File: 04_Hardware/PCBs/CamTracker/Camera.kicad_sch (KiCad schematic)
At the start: 29 parts, among them J11 22-28-4034, J12 22-28-4034, J8 20021521-00016T1LF, J9 20021521-00016T1LF, U1 SC206EEMDA-G51-UGNDA

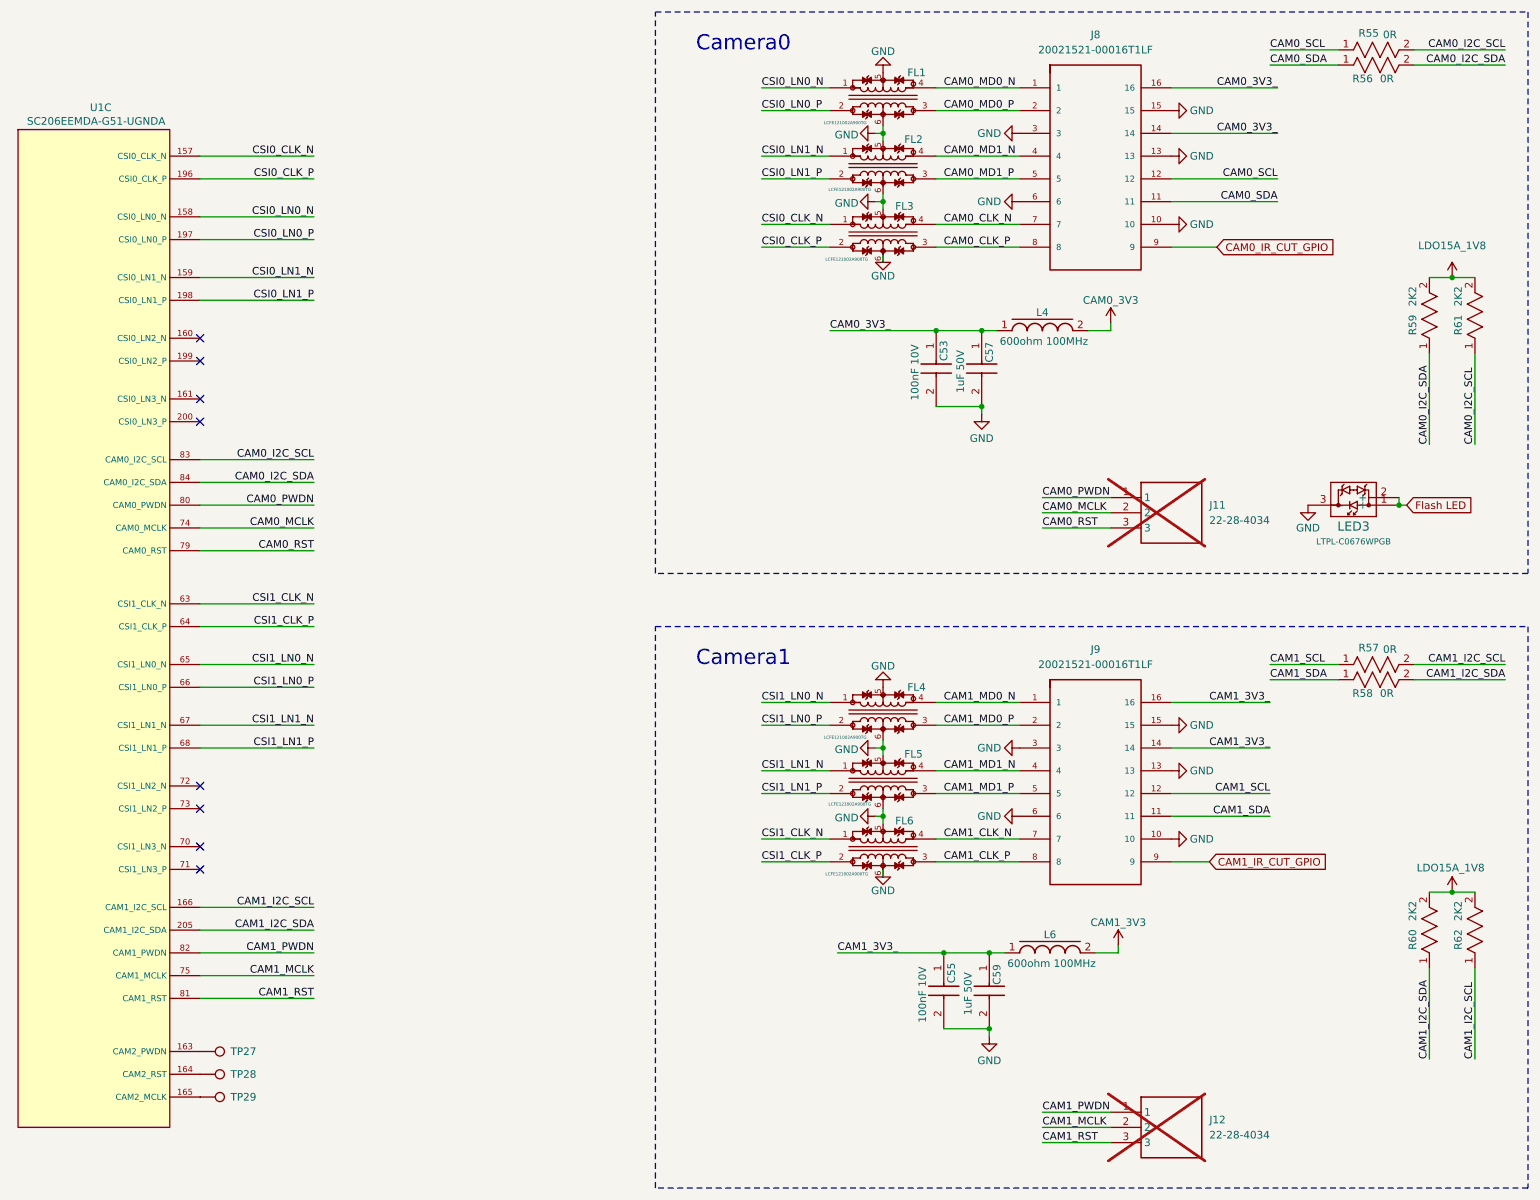
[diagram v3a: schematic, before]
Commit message: feat(PCB): Cam Connectors have been changed with 2x10P
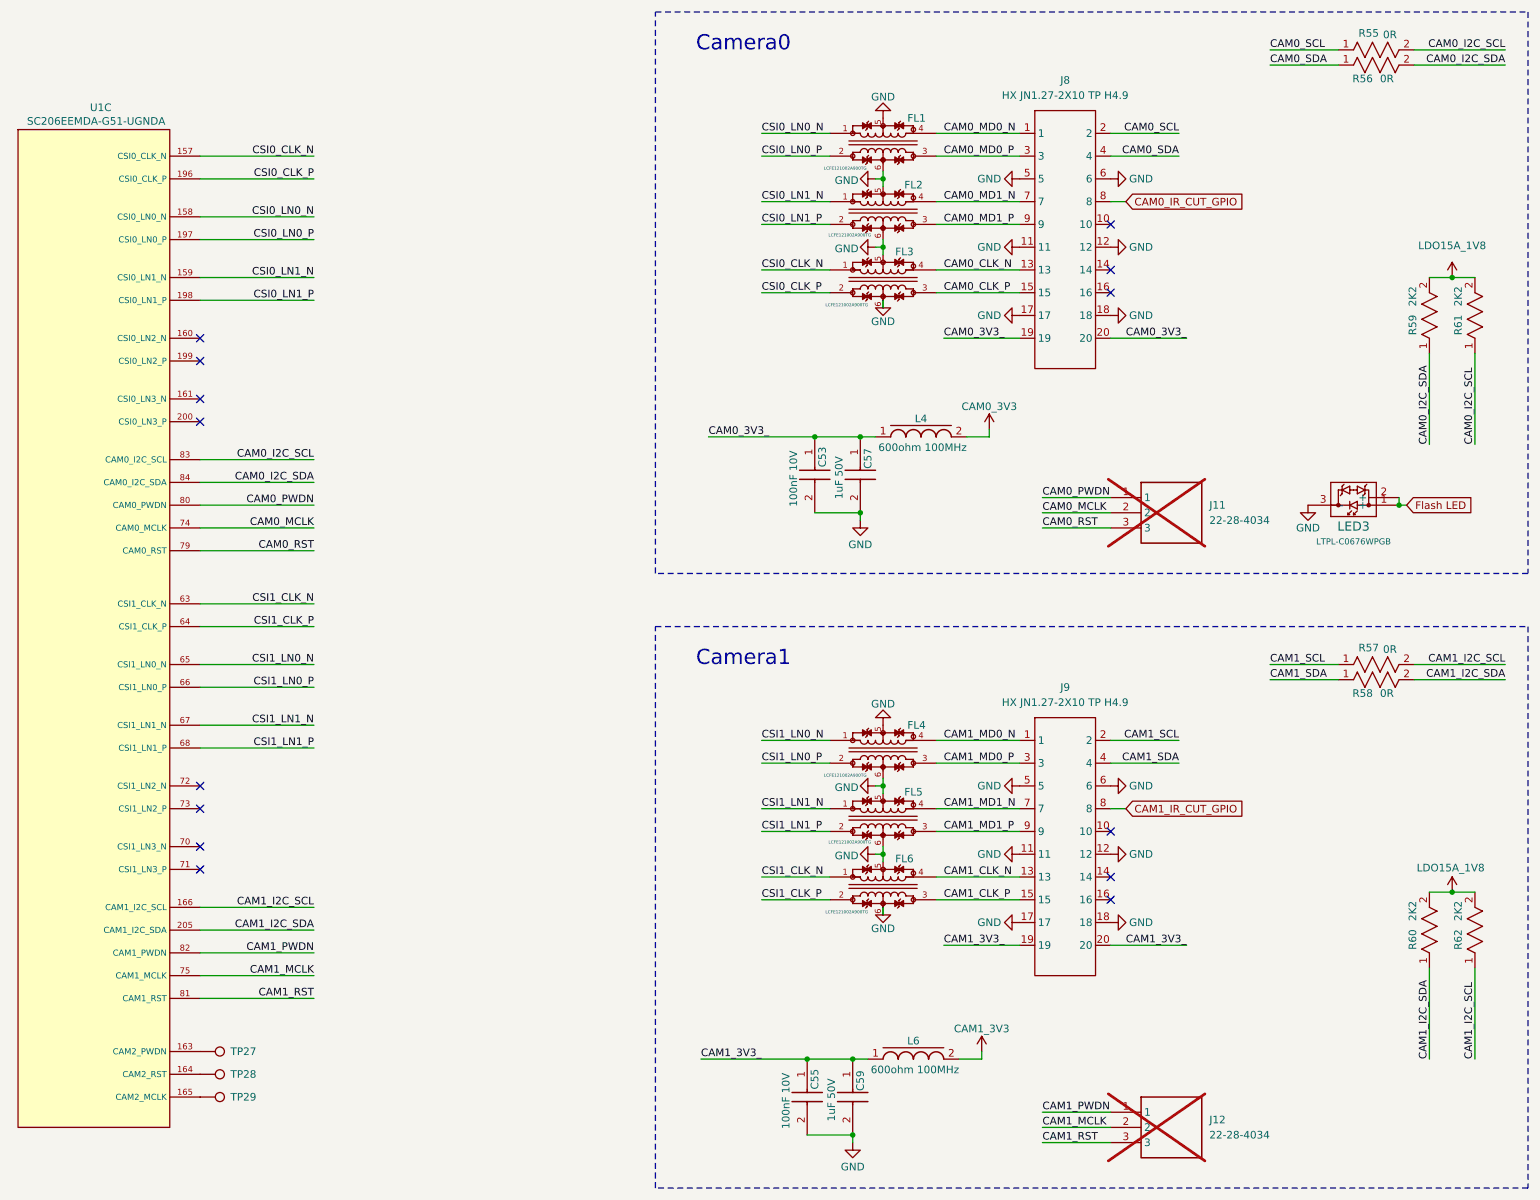
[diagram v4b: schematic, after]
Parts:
- removed J8, J9: 20021521-00016T1LF, 000MCLib:AMPHENOL_20021521-00016T1LF, symbol 000MCLib:20021521-00016T1LF
- added J8, J9: HX JN1.27-2X10 TP H4.9, 000MCLib:CONN-SMD_HX-JN1.27-2X10-TP-H4.9, symbol 000MCLib:HX JN1.27-2X10 TP H4.9
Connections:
- net CAM0_3V3_: now also J8.19, J8.20
- net CAM0_CLK_N: now also J8.13
- net CAM0_CLK_P: now also J8.15
- net CAM0_IR_CUT_GPIO: now also J8.8
- net CAM0_MD0_N: now also J8.1
- net CAM0_MD0_P: now also J8.3
- net CAM0_MD1_N: now also J8.7
- net CAM0_MD1_P: now also J8.9
- net CAM0_SCL: now also J8.2
- net CAM0_SDA: now also J8.4
- net CAM1_3V3_: now also J9.19, J9.20
- net CAM1_CLK_N: now also J9.13
- net CAM1_CLK_P: now also J9.15
- net CAM1_IR_CUT_GPIO: now also J9.8
- net CAM1_MD0_N: now also J9.1
- net CAM1_MD0_P: now also J9.3
- net CAM1_MD1_N: now also J9.7
- net CAM1_MD1_P: now also J9.9
- net CAM1_SCL: now also J9.2
- net CAM1_SDA: now also J9.4
- net GND: now also J8.11, J8.12, J8.17, J8.18, J8.5, J8.6, J9.11, J9.12, J9.17, J9.18, J9.5, J9.6
- no-connect marks 8 -> 14
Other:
- moved on the sheet: C53, C55, C57, C59, FL1, FL2, FL3, FL4, FL5, FL6, L4, L6

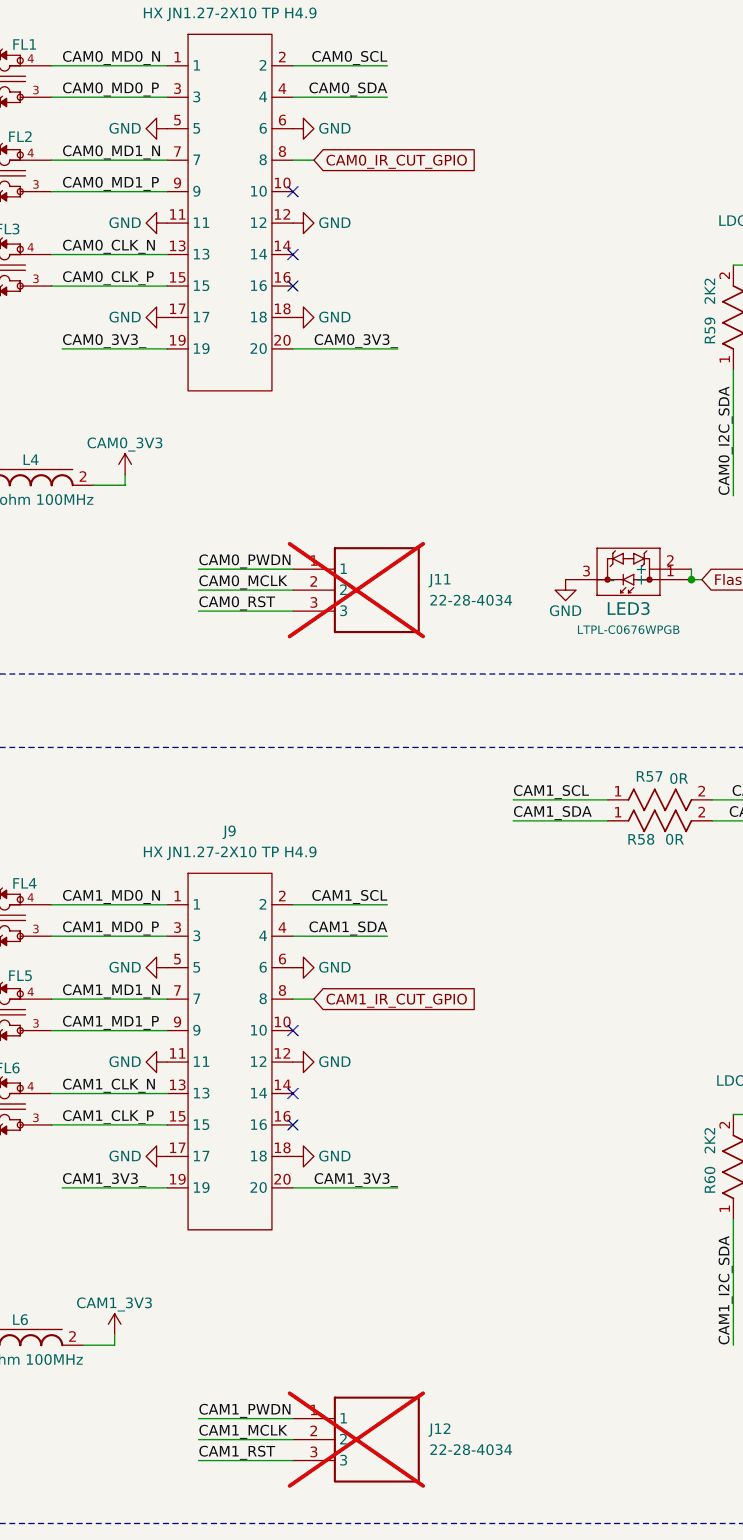
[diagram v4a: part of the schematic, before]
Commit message: feat(PCB): finalize PCB design and generate BOM/Gerbers
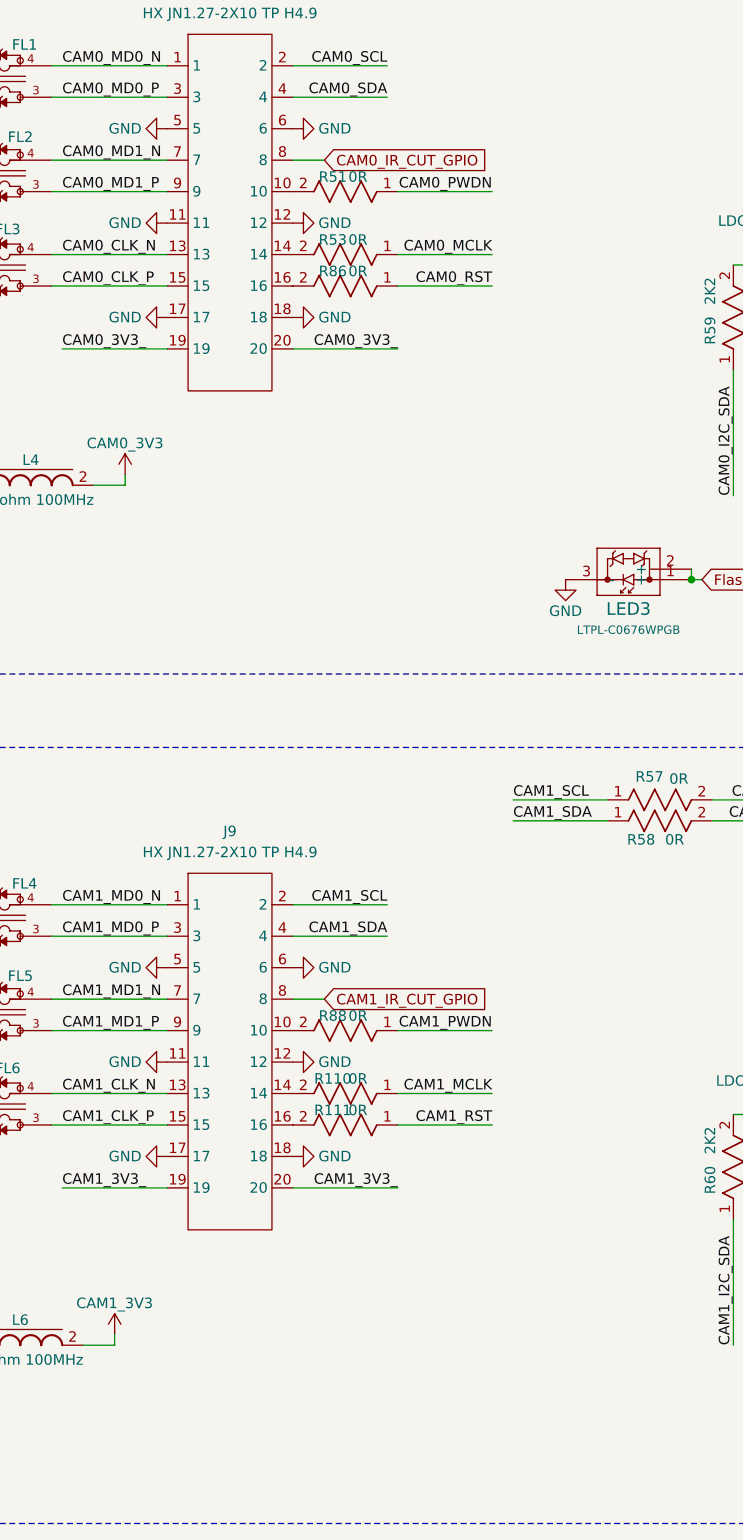
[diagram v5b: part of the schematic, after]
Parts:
- removed J11, J12: 22-28-4034, 000MCLib:HDRV3W66P0X254_1X3_762X249X1042P, symbol 000MCLib:22-28-4034
- added R110, R111, R51, R53, R86, R88: 0R, 000MCLib:RC0402N_YAG, symbol 000MCLib:RC0402JR-070RL
- J8, J9: Manufacturer Part HX JN1.27-2x10 TP H4.9 -> (none); Part Number (none) -> HX JN1.27-2x10 TP H4.9
- R55, R56, R57, R58: Height 0.5 -> (none); Mouser Part Number 71-CRCW0805-0-E3 -> (none); Mouser Price/Stock https://www.mouser.co.uk/ProductDetail/Vishay-Dale/CRCW0805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 -> (none)
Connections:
- net CAM0_MCLK: now also R53.1
- net CAM0_PWDN: now also R51.1
- net CAM0_RST: now also R86.1
- net CAM1_MCLK: now also R110.1
- net CAM1_PWDN: now also R88.1
- net CAM1_RST: now also R111.1
- net at J9.10: now also R88.2
- net at J9.14: now also R110.2
- net at J9.16: now also R111.2
- net at J8.10: now also R51.2
- net at J8.14: now also R53.2
- net at J8.16: now also R86.2
- no-connect marks 14 -> 8
